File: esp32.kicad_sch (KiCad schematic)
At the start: 12 parts, among them J2 Conn_01x06_Pin, SW1 BOOT, U6 ESP32-WROOM-32, U7 CMXT3904

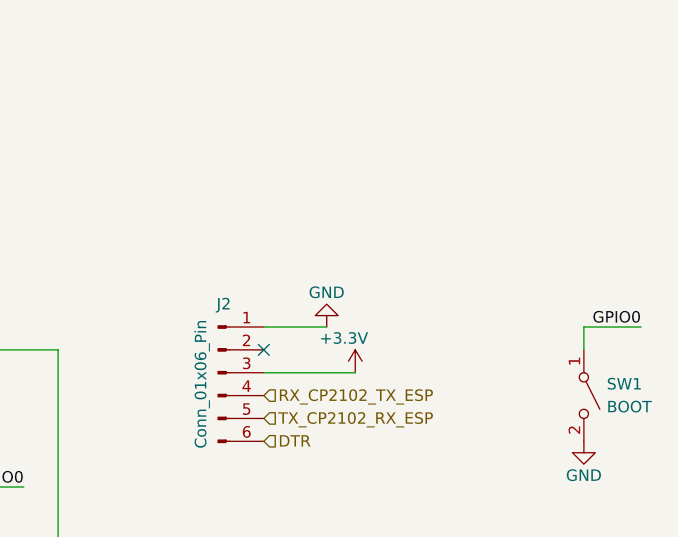
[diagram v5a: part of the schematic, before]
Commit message: added jumper to FTDI power
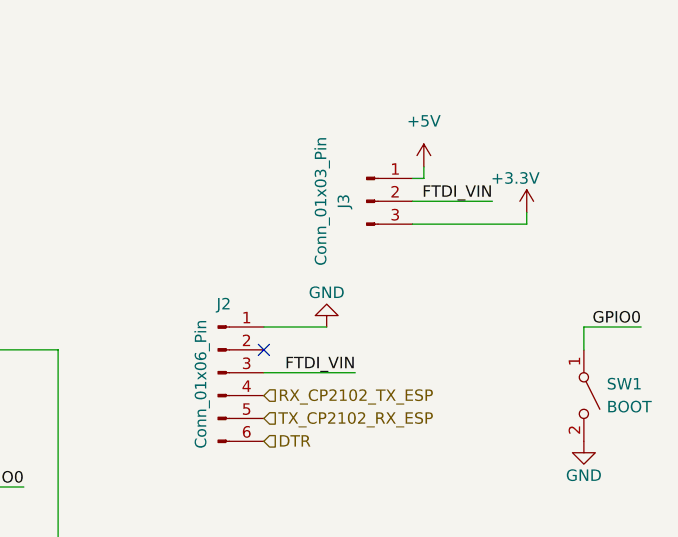
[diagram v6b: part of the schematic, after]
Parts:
- added J3: Conn_01x03_Pin, Connector_PinHeader_2.54mm:PinHeader_1x03_P2.54mm_Vertical, symbol Connector:Conn_01x03_Pin
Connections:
- net +3.3V: now also J3.3 (Pin_3); no longer J2.3 (Pin_3)
- new net +5V: J3.1 (Pin_1)
- new net FTDI_VIN: J2.3 (Pin_3), J3.2 (Pin_2)
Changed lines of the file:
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@@
+    (stroke (width 0) (type default))
+  )
+  (wire (pts (xy 209.55 55.88) (xy 209.55 54.61))
     (stroke (width 0) (type default))
   )
@@
     (stroke (width 0) (type default))
   )
+  (wire (pts (xy 208.28 58.42) (xy 217.17 58.42))
+    (stroke (width 0) (type default))
+  )
   (wire (pts (xy 148.59 71.12) (xy 148.59 74.93))
     (stroke (width 0) (type default))
@@
     (stroke (width 0) (type default))
   )
+  (wire (pts (xy 220.98 59.69) (xy 220.98 60.96))
+    (stroke (width 0) (type default))
+  )
   (wire (pts (xy 96.52 50.8) (xy 96.52 52.07))
     (stroke (width 0) (type default))
   )
   (wire (pts (xy 90.17 57.15) (xy 110.49 57.15))
+    (stroke (width 0) (type default))
+  )
+  (wire (pts (xy 209.55 55.88) (xy 208.28 55.88))
+    (stroke (width 0) (type default))
+  )
+  (wire (pts (xy 220.98 60.96) (xy 208.28 60.96))
     (stroke (width 0) (type default))
   )
@@
     (effects (font (size 1.27 1.27)) (justify left bottom))
   )
+  (label "FTDI_VIN" (at 217.17 58.42 180) (fields_autoplaced)
+    (effects (font (size 1.27 1.27)) (justify right bottom))
+  )
   (label "RESETn" (at 125.73 74.93 0) (fields_autoplaced)
     (effects (font (size 1.27 1.27)) (justify left bottom))
   )
+  (label "FTDI_VIN" (at 201.93 77.47 180) (fields_autoplaced)
+    (effects (font (size 1.27 1.27)) (justify right bottom))
+  )
   (hierarchical_label "TX_CP2102_RX_ESP" (shape input) (at 45.72 82.55 180) (fields_autoplaced)
     (effects (font (size 1.27 1.27)) (justify right))
@@
         (path "/955dc1f6-0512-416a-b86b-95ec08ff77cb/ecc56fd3-dc72-490a-a501-0be3de98d0c1"
           (reference "#PWR021") (unit 1)
+        )
+      )
+    )
+  )
+  (symbol (lib_id "power:+3.3V") (at 220.98 59.69 0) (unit 1)
+    (in_bom yes) (on_board yes) (dnp no)
+    (property "Reference" "#PWR023" (at 220.98 63.5 0)
+      (effects (font (size 1.27 1.27)) hide)
+    )
+    (property "Value" "+3.3V" (at 219.71 55.88 0)
+      (effects (font (size 1.27 1.27)))
+    )
+    (property "Footprint" "" (at 220.98 59.69 0)
+      (effects (font (size 1.27 1.27)) hide)
+    )
+    (property "Datasheet" "" (at 220.98 59.69 0)
+      (effects (font (size 1.27 1.27)) hide)
+    )
+    (pin "1")
+    (instances
+      (project "RGB LED Driver"
+        (path "/955dc1f6-0512-416a-b86b-95ec08ff77cb/ecc56fd3-dc72-490a-a501-0be3de98d0c1"
+          (reference "#PWR023") (unit 1)
         )
       )
@@
     )
   )
+  (symbol (lib_id "Connector:Conn_01x03_Pin") (at 203.2 58.42 0) (unit 1)
+    (in_bom yes) (on_board yes) (dnp no) (fields_autoplaced)
+    (property "Reference" "J3" (at 200.66 58.42 90)
+      (effects (font (size 1.27 1.27)))
+    )
+    (property "Value" "Conn_01x03_Pin" (at 198.12 58.42 90)
+      (effects (font (size 1.27 1.27)))
+    )
+    (property "Footprint" "Connector_PinHeader_2.54mm:PinHeader_1x03_P2.54mm_Vertical" (at 203.2 58.42 0)
+      (effects (font (size 1.27 1.27)) hide)
+    )
+    (property "Datasheet" "~" (at 203.2 58.42 0)
+      (effects (font (size 1.27 1.27)) hide)
+    )
+    (pin "1")
+    (pin "2")
+    (pin "3")
+    (instances
+      (project "RGB LED Driver"
+        (path "/955dc1f6-0512-416a-b86b-95ec08ff77cb/ecc56fd3-dc72-490a-a501-0be3de98d0c1"
+          (reference "J3") (unit 1)
+        )
+      )
+    )
+  )
   (symbol (lib_id "Device:C") (at 96.52 48.26 0) (unit 1)
     (in_bom yes) (on_board yes) (dnp no) (fields_autoplaced)
@@
         (path "/955dc1f6-0512-416a-b86b-95ec08ff77cb/ecc56fd3-dc72-490a-a501-0be3de98d0c1"
           (reference "#PWR07") (unit 1)
+        )
+      )
+    )
+  )
+  (symbol (lib_id "power:+5V") (at 209.55 54.61 0) (unit 1)
+    (in_bom yes) (on_board yes) (dnp no) (fields_autoplaced)
+    (property "Reference" "#PWR055" (at 209.55 58.42 0)
+      (effects (font (size 1.27 1.27)) hide)
+    )
+    (property "Value" "+5V" (at 209.55 49.53 0)
+      (effects (font (size 1.27 1.27)))
+    )
+    (property "Footprint" "" (at 209.55 54.61 0)
+      (effects (font (size 1.27 1.27)) hide)
+    )
+    (property "Datasheet" "" (at 209.55 54.61 0)
+      (effects (font (size 1.27 1.27)) hide)
+    )
+    (pin "1")
+    (instances
+      (project "RGB LED Driver"
+        (path "/955dc1f6-0512-416a-b86b-95ec08ff77cb/ecc56fd3-dc72-490a-a501-0be3de98d0c1"
+          (reference "#PWR055") (unit 1)
         )
       )
@@
         )
       )
-    )
-  )
-  (symbol (lib_id "power:+3.3V") (at 201.93 77.47 0) (unit 1)
-    (in_bom yes) (on_board yes) (dnp no)
-    (property "Reference" "#PWR023" (at 201.93 81.28 0)
-      (effects (font (size 1.27 1.27)) hide)
-    )
-    (property "Value" "+3.3V" (at 200.66 73.66 0)
-      (effects (font (size 1.27 1.27)))
-    )
-    (property "Footprint" "" (at 201.93 77.47 0)
-      (effects (font (size 1.27 1.27)) hide)
-    )
-    (property "Datasheet" "" (at 201.93 77.47 0)
-      (effects (font (size 1.27 1.27)) hide)
-    )
-    (pin "1")
-    (instances
-      (project "RGB LED Driver"
-        (path "/955dc1f6-0512-416a-b86b-95ec08ff77cb/ecc56fd3-dc72-490a-a501-0be3de98d0c1"
-          (reference "#PWR023") (unit 1)
-        )
-      )

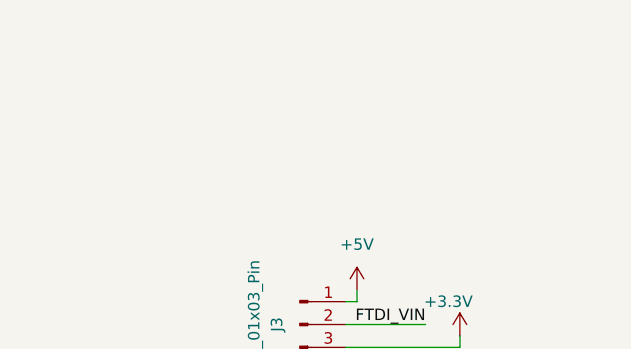
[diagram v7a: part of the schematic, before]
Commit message: Added jumper into BOM
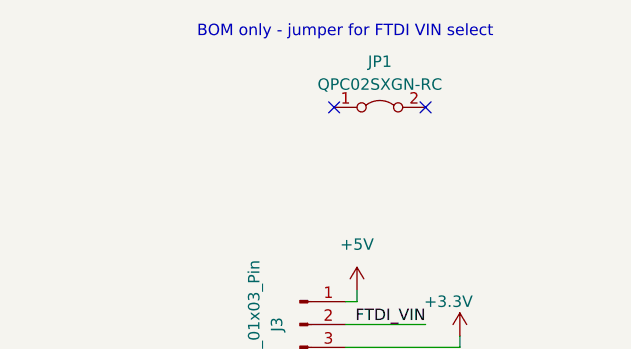
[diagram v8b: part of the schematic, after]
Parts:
- added JP1: QPC02SXGN-RC, symbol Jumper:Jumper_2_Bridged
- J2: Digikey PN (none) -> 2057-PH1-06-UA-ND; MPN (none) -> PH1-06-UA
- J3: Digikey PN (none) -> 2057-PH1-03-UA-ND; MPN (none) -> PH1-03-UA
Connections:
- no-connect marks 25 -> 27
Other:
- note added: "BOM only - jumper for FTDI VIN select"
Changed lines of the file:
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@@
   (no_connect (at 49.53 67.31))
   (no_connect (at 90.17 62.23))
+  (no_connect (at 207.01 34.29))
   (no_connect (at 49.53 105.41))
   (no_connect (at 90.17 59.69))
@@
   (no_connect (at 90.17 64.77))
   (no_connect (at 49.53 72.39))
+  (no_connect (at 217.17 34.29))
   (no_connect (at 90.17 69.85))
   (no_connect (at 90.17 74.93))
@@
     (stroke (width 0) (type default))
   )
+  (text "BOM only - jumper for FTDI VIN select" (at 191.77 26.67 0)
+    (effects (font (size 1.27 1.27)) (justify left bottom))
+  )
   (label "GPIO0" (at 233.68 72.39 180) (fields_autoplaced)
     (effects (font (size 1.27 1.27)) (justify right bottom))
@@
         (path "/955dc1f6-0512-416a-b86b-95ec08ff77cb/ecc56fd3-dc72-490a-a501-0be3de98d0c1"
           (reference "R11") (unit 1)
+        )
+      )
+    )
+  )
+  (symbol (lib_id "Jumper:Jumper_2_Bridged") (at 212.09 34.29 0) (unit 1)
+    (in_bom yes) (on_board no) (dnp no) (fields_autoplaced)
+    (property "Reference" "JP1" (at 212.09 29.21 0)
+      (effects (font (size 1.27 1.27)))
+    )
+    (property "Value" "QPC02SXGN-RC" (at 212.09 31.75 0)
+      (effects (font (size 1.27 1.27)))
+    )
+    (property "Footprint" "" (at 212.09 34.29 0)
+      (effects (font (size 1.27 1.27)) hide)
+    )
+    (property "Datasheet" "~" (at 212.09 34.29 0)
+      (effects (font (size 1.27 1.27)) hide)
+    )
+    (property "Digikey PN" "S9337-ND" (at 212.09 34.29 0)
+      (effects (font (size 1.27 1.27)) hide)
+    )
+    (property "MPN" "QPC02SXGN-RC" (at 212.09 34.29 0)
+      (effects (font (size 1.27 1.27)) hide)
+    )
+    (pin "1")
+    (pin "2")
+    (instances
+      (project "RGB LED Driver"
+        (path "/955dc1f6-0512-416a-b86b-95ec08ff77cb/ecc56fd3-dc72-490a-a501-0be3de98d0c1"
+          (reference "JP1") (unit 1)
         )
       )
@@
       (effects (font (size 1.27 1.27)) hide)
     )
+    (property "Digikey PN" "2057-PH1-03-UA-ND" (at 203.2 58.42 0)
+      (effects (font (size 1.27 1.27)) hide)
+    )
+    (property "MPN" "PH1-03-UA" (at 203.2 58.42 0)
+      (effects (font (size 1.27 1.27)) hide)
+    )
     (pin "1")
     (pin "2")
@@
       (effects (font (size 1.27 1.27)) hide)
     )
-    (property "Digikey PN" "" (at 186.69 77.47 0)
-      (effects (font (size 1.27 1.27)) hide)
-    )
+    (property "Digikey PN" "2057-PH1-06-UA-ND" (at 186.69 77.47 0)
+      (effects (font (size 1.27 1.27)) hide)
+    )
+    (property "MPN" "PH1-06-UA" (at 186.69 77.47 0)
+      (effects (font (size 1.27 1.27)) hide)
+    )
